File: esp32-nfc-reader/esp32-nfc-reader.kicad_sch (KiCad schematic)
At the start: 50 parts, among them J1 USB_C_Receptacle_USB2.0_16P, J2 Conn_01x02_Pin, J3 Conn_01x08, K1 Relay_SPDT, Q1 PMOS, Q2 Q_NMOS, SW1 RESET, SW2 BOOT, SW3 USER_INPUT, U1 ESP32-S3-WROOM-1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

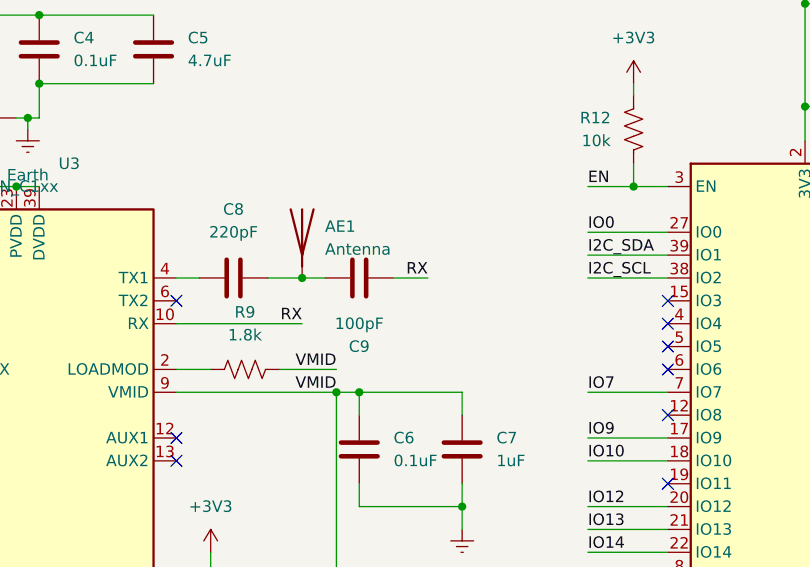
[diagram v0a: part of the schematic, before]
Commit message: added antenna loop
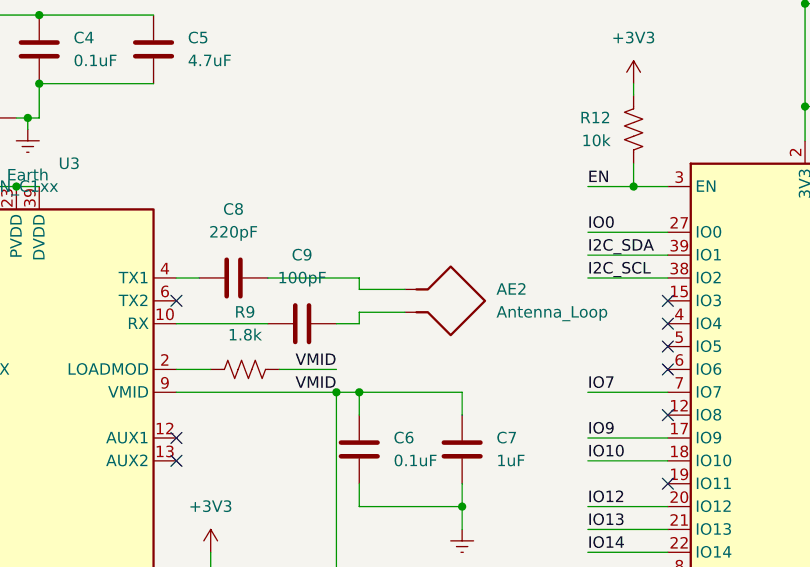
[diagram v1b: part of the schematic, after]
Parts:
- removed AE1: Antenna, Connector_PinSocket_2.54mm:PinSocket_1x01_P2.54mm_Vertical, symbol Device:Antenna
- added AE2: Antenna_Loop, RF_Antenna:Coilcraft_MA5532-AE_RFID, symbol Device:Antenna_Loop
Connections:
- net at C8.2: now also AE2.1; no longer C9.1
- net RX: no longer names the net of C9.2, U3.10 (RX)
- new net: AE2.2, C9.1
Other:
- moved on the sheet: C9
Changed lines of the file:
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@@
 	)
 	(junction
-		(at 191.77 60.96)
-		(diameter 0)
-		(color 0 0 0 0)
-	)
-	(junction
 		(at 157.48 116.84)
 		(diameter 0)
@@
 	(wire
 		(pts
+			(xy 198.12 60.96) (xy 198.12 62.23)
+		)
+		(stroke
+			(width 0)
+			(type default)
+		)
+	)
+	(wire
+		(pts
 			(xy 135.89 157.48) (xy 142.24 157.48)
 		)
@@
 	(wire
 		(pts
+			(xy 203.2 64.77) (xy 198.12 64.77)
+		)
+		(stroke
+			(width 0)
+			(type default)
+		)
+	)
+	(wire
+		(pts
 			(xy 177.8 73.66) (xy 195.58 73.66)
 		)
@@
 	(wire
 		(pts
-			(xy 191.77 60.96) (xy 194.31 60.96)
+			(xy 27.94 152.4) (xy 31.75 152.4)
 		)
 		(stroke
@@
 	(wire
 		(pts
-			(xy 27.94 152.4) (xy 31.75 152.4)
+			(xy 50.8 34.29) (xy 55.88 34.29)
 		)
 		(stroke
@@
 	(wire
 		(pts
-			(xy 50.8 34.29) (xy 55.88 34.29)
+			(xy 177.8 96.52) (xy 181.61 96.52)
 		)
 		(stroke
@@
 	(wire
 		(pts
-			(xy 177.8 96.52) (xy 181.61 96.52)
+			(xy 149.86 157.48) (xy 152.4 157.48)
 		)
 		(stroke
@@
 	(wire
 		(pts
-			(xy 149.86 157.48) (xy 152.4 157.48)
+			(xy 198.12 62.23) (xy 203.2 62.23)
 		)
 		(stroke
@@
 	(wire
 		(pts
+			(xy 187.96 60.96) (xy 198.12 60.96)
+		)
+		(stroke
+			(width 0)
+			(type default)
+		)
+	)
+	(wire
+		(pts
 			(xy 127 73.66) (xy 137.16 73.66)
 		)
@@
 	(wire
 		(pts
-			(xy 201.93 60.96) (xy 205.74 60.96)
+			(xy 198.12 66.04) (xy 195.58 66.04)
 		)
 		(stroke
@@
 	(wire
 		(pts
-			(xy 209.55 86.36) (xy 209.55 88.9)
+			(xy 198.12 64.77) (xy 198.12 66.04)
 		)
 		(stroke
@@
 	(wire
 		(pts
-			(xy 177.8 66.04) (xy 191.77 66.04)
+			(xy 209.55 86.36) (xy 209.55 88.9)
 		)
 		(stroke
@@
 	(wire
 		(pts
-			(xy 261.62 138.43) (xy 261.62 139.7)
+			(xy 177.8 66.04) (xy 187.96 66.04)
 		)
 		(stroke
@@
 	(wire
 		(pts
-			(xy 247.65 101.6) (xy 247.65 104.14)
+			(xy 261.62 138.43) (xy 261.62 139.7)
 		)
 		(stroke
@@
 	(wire
 		(pts
-			(xy 187.96 60.96) (xy 191.77 60.96)
+			(xy 247.65 101.6) (xy 247.65 104.14)
 		)
 		(stroke
@@
 		)
 	)
-	(label "RX"
-		(at 191.77 66.04 180)
-		(effects
-			(font
-				(size 1.27 1.27)
-			)
-			(justify right bottom)
-		)
-	)
 	(label "USB_DP"
 		(at 271.78 63.5 180)
@@
 		)
 	)
-	(label "RX"
-		(at 205.74 60.96 180)
-		(effects
-			(font
-				(size 1.27 1.27)
-			)
-			(justify right bottom)
-		)
-	)
 	(label "IO12"
 		(at 223.52 86.36 0)
@@
 	)
 	(symbol
+		(lib_id "Device:Antenna_Loop")
+		(at 208.28 62.23 270)
+		(unit 1)
+		(exclude_from_sim no)
+		(in_bom yes)
+		(on_board yes)
+		(dnp no)
+		(fields_autoplaced yes)
+		(property "Reference" "AE2"
+			(at 213.36 62.2299 90)
+			(effects
+				(font
+					(size 1.27 1.27)
+				)
+				(justify left)
+			)
+		)
+		(property "Value" "Antenna_Loop"
+			(at 213.36 64.7699 90)
+			(effects
+				(font
+					(size 1.27 1.27)
+				)
+				(justify left)
+			)
+		)
+		(property "Footprint" "RF_Antenna:Coilcraft_MA5532-AE_RFID"
+			(at 208.28 62.23 0)
+			(effects
+				(font
+					(size 1.27 1.27)
+				)
+				(hide yes)
+			)
+		)
+		(property "Datasheet" "~"
+			(at 208.28 62.23 0)
+			(effects
+				(font
+					(size 1.27 1.27)
+				)
+				(hide yes)
+			)
+		)
+		(property "Description" "Loop antenna"
+			(at 208.28 62.23 0)
+			(effects
+				(font
+					(size 1.27 1.27)
+				)
+				(hide yes)
+			)
+		)
+		(pin "1"
+		)
+		(pin "2"
+		)
+		(instances
+			(project ""
+				(path "/06ef8056-7982-4b5f-a4e7-c1b452db5ec6"
+					(reference "AE2")
+					(unit 1)
+				)
+			)
+		)
+	)
+	(symbol
 		(lib_id "power:+3V3")
 		(at 82.55 167.64 0)
@@
 	)
 	(symbol
-		(lib_id "Device:Antenna")
-		(at 191.77 55.88 0)
-		(unit 1)
-		(exclude_from_sim no)
-		(in_bom yes)
-		(on_board yes)
-		(dnp no)
-		(fields_autoplaced yes)
-		(property "Reference" "AE1"
-			(at 194.31 55.2449 0)
-			(effects
-				(font
-					(size 1.27 1.27)
-				)
-				(justify left)
-			)
-		)
-		(property "Value" "Antenna"
-			(at 194.31 57.7849 0)
-			(effects
-				(font
-					(size 1.27 1.27)
-				)
-				(justify left)
-			)
-		)
-		(property "Footprint" "Connector_PinSocket_2.54mm:PinSocket_1x01_P2.54mm_Vertical"
-			(at 191.77 55.88 0)
-			(effects
-				(font
-					(size 1.27 1.27)
-				)
-				(hide yes)
-			)
-		)
-		(property "Datasheet" "~"
-			(at 191.77 55.88 0)
-			(effects
-				(font
-					(size 1.27 1.27)
-				)
-				(hide yes)
-			)
-		)
-		(property "Description" "Antenna"
-			(at 191.77 55.88 0)
-			(effects
-				(font
-					(size 1.27 1.27)
-				)
-				(hide yes)
-			)
-		)
-		(pin "1"
-		)
-		(instances
-			(project ""
-				(path "/06ef8056-7982-4b5f-a4e7-c1b452db5ec6"
-					(reference "AE1")
-					(unit 1)
-				)
-			)
-		)
-	)
-	(symbol
 		(lib_id "Device:R_US")
 		(at 26.67 109.22 90)
@@
 	(symbol
 		(lib_id "Device:C")
-		(at 198.12 60.96 90)
+		(at 191.77 66.04 270)
 		(mirror x)
 		(unit 1)
@@
 		(dnp no)
 		(property "Reference" "C9"
-			(at 198.12 68.58 90)
+			(at 191.77 58.42 90)
 			(effects
 				(font
@@
 		)
 		(property "Value" "100pF"
-			(at 198.12 66.04 90)
+			(at 191.77 60.96 90)
 			(effects
 				(font
@@
 		)
 		(property "Footprint" "Capacitor_SMD:C_0402_1005Metric"
-			(at 201.93 61.9252 0)
+			(at 187.96 65.0748 0)
 			(effects
 				(font
@@
 		)
 		(property "Datasheet" "~"
-			(at 198.12 60.96 0)
+			(at 191.77 66.04 0)
 			(effects
 				(font
@@
 		)
 		(property "Description" "Unpolarized capacitor"
-			(at 198.12 60.96 0)
+			(at 191.77 66.04 0)
 			(effects
 				(font
